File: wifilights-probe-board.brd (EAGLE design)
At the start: 50.8 x 50.8 mm, 48 parts, among them Q1 BUK98180-100A, Q2 BUK98180-100A, Q3 BUK98180-100A, Q4 BUK98180-100A, U2 PCA9685

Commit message: Probe board complete
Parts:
- removed A, B: (no value), adafruit:1X01
- removed B2: DBLS203G, rectifier:DBS
- removed C3: 220pf, resistor:C0805K
- removed C4, C6: 0.1uF, resistor:C0805K
- removed C7: 10uF, resistor:C0805K
- removed D1: MBRS140T3, diode:SMB
- removed L1: 220uf, SparkFun-Passives:SDR0403
- removed LED3: OVSTRGBBCR8, led:OVSTRGBBCR8
- removed MPU: ESP8266_ESP-12, ESP8266-ESP12:ESP8266-ESP12
- removed PWR, THINKING: (no value), led:CHIP-LED0805
- removed Q1, Q2, Q3, Q4: BUK98180-100A, nxp_60:SOT223
- removed R4: 1K, resistor:R0805
- removed R5, R6: 1k, resistor:R0805
- removed R7: ???, resistor:R0805
- removed R8: 10K, resistor:R0805
- removed REG1: MC33063/MC34063D, adafruit:SO08
- removed REG2: MC33269-SO8, linear:SO08
- removed TEMPERATURE: MPL3115A2LGA8, SparkFun-Sensors:LGA8
- removed U$1, U$2, U$3: LUXEON-REBEL, SparkFun-LED:LUXEON-REBEL
- removed U2: PCA9685, adafruit:TSSOP28
- added F1: 500mA, SparkFun:PTC-1206
- added H2, H3, H4, H5: SEW_HOLE, LilyPad-Wearables:SIMPLE_HOLE
- added J1: 22-05-7028-02, con-molex:7395-02
- added JP1: (no value), SparkFun-Connectors:2X5-SHROUDED
- added JP7: USB_MICROB_PLUGCONN-11752, SparkFun-Connectors:USB-B-MICRO-SMD_V03
- added S1: SWITCH-MOMENTARY-2PTH, SparkFun-Electromechanical:TACTILE-PTH
- added TPCHPD, TPGPIO0, TPGPIO2, TPRX, TPTX: (no value), SparkFun-Connectors:1X01_POGOPIN_HOLE_0.58
- added U1: FT232R, SparkFun:SSOP28DB
- C1, C2: device resistor:C0805K -> SparkFun-Capacitors:0603-CAP
- LED1: value OVSTRGBBCR8 -> Red; device led:OVSTRGBBCR8 -> SparkFun-LED:LED-0603
- LED2: value OVSTRGBBCR8 -> Green; device led:OVSTRGBBCR8 -> SparkFun-LED:LED-0603
- P_RED, P_WHITE, RED, SCL, SDA, TP12V, TP3.3V, TP5V, TPGND, WHITE: value TEST-POINT3X5 -> (none); device SparkFun-Passives:PAD.03X.05 -> SparkFun-Connectors:1X01_POGOPIN_HOLE_0.58
- R1: value 220 ??? -> 330; device resistor:R0805 -> SparkFun-Resistors:0603-RES
- R2: value ??? -> 330; device resistor:R0805 -> SparkFun-Resistors:0603-RES
- R3: value 3K -> 1k; device resistor:R0805 -> SparkFun-Passives:AXIAL-0.3
- moved C5 48.8 mm to (49.7, 41.9), flipped to the top, turned to 0 degrees
- moved LED1 39.5 mm to (49.7, 36.8), flipped to the top, turned to 90 degrees
- moved R2 37.2 mm to (49.5, 28.9), flipped to the top, turned to 270 degrees
- moved R1 35.4 mm to (51.8, 28.9), turned to 270 degrees
- moved C2 17.1 mm to (49.7, 44.6), turned to 180 degrees
- moved C1 11.1 mm to (47.5, 28.9), flipped to the top
- moved LED2 9.34 mm to (49.7, 35.6), flipped to the top, turned to 90 degrees
- moved TP3.3V 4.07 mm to (19.7, 24.9)
- moved R3 2.58 mm to (22.5, 20.2), turned to 90 degrees
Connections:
- removed net BLUE: Q2.1, U2.7
- removed net COMP: R3.2, R4.1, REG1.5
- removed net GREEN: Q4.1, U2.9
- removed net N$10: U$1.CATHODE, U$2.ANODE
- removed net N$11: U$2.CATHODE, U$3.ANODE
- removed net N$13: R1.2, REG1.1, REG1.7, REG1.8
- removed net N$14: PWR.A, R2.2
- removed net N$15: R7.2, THINKING.A
- removed net N$16: C3.1, REG1.3
- removed net N$17: C4.1, TEMPERATURE.2
- removed net N$18: A.1, B2.AC1
- removed net N$19: B.1, B2.AC2
- removed net N$20: R8.2, U2.23
- removed net N$25: MPU.13
- removed net N$26: MPU.12
- removed net N$27: MPU.11
- removed net N$28: MPU.10
- removed net N$29: MPU.9
- removed net N$32: MPU.6
- removed net N$33: MPU.4
- removed net N$34: MPU.3
- removed net N$35: MPU.2
- removed net N$36: MPU.5
- removed net N$5: LED2.5, LED2.5@1, LED3.2
- removed net N$6: LED1.5, LED1.5@1, LED2.2
- removed net N$7: LED1.6, LED1.6@1, LED2.3
- removed net N$8: LED2.6, LED2.6@1, LED3.3
- removed net P_BLUE: LED3.6, LED3.6@1, Q2.2, Q2.4
- removed net P_GREEN: LED3.4, LED3.4@1, Q4.2, Q4.4
- removed net RESET: MPU.8
- removed net SWE: D1.C, L1.P$2, REG1.2
- removed net THINKING: MPU.7, R7.1
- new net CTS: U1.11
- new net DCD: U1.10
- new net DSR: U1.9
- new net DTR: U1.2
- new net GPIO0: R3.P$1, S1.3, TPGPIO0.1
- new net N$3: F1.1, JP7.VBUS1
- new net PWREN: U1.14
- new net RI: U1.6
- new net RTS: U1.3
- new net RXD: TPRX.1, U1.5
- new net RXLED: LED2.C, U1.22
- new net SLEEP: U1.12
- new net TXD: TPTX.1, U1.1
- new net TXDEN: U1.13
- new net TXLED: LED1.C, U1.23
- new net USB_D+: JP7.D+1, U1.15
- new net USB_D-: JP7.D-1, U1.16
- new net VCC: C2.1, C5.A, F1.2, U1.20
- net 12V: now also J1.1, TP12V.1; no longer B2.+, LED1.1, LED1.2, LED1.3, R1.1, REG1.6, TP12V.P$1, U$1.ANODE
- net 3.3V: now also JP1.2, R1.2, R2.2, R3.P$2, TP3.3V.1, TPCHPD.1, TPGPIO2.1, U1.17, U1.4; no longer C2.1, C7.1, MPU.16, R2.1, R5.2, R6.2, REG2.2, REG2.3, REG2.6, REG2.7, TEMPERATURE.1, TEMPERATURE.4, TP3.3V.P$1, U2.28
- net 5V: now also JP1.1, TP5V.1; no longer C5.A, C6.1, L1.P$1, R3.1, REG2.4, TP5V.P$1
- net GND: now also H2.P$1, H3.P$1, H4.P$1, H5.P$1, J1.2, JP1.10, JP1.9, JP7.GND1, S1.1, TPGND.1, U1.18, U1.21, U1.25, U1.26, U1.7; no longer B2.-, C3.2, C4.2, C6.2, C7.2, D1.A, MPU.1, PWR.C, Q1.3, Q2.3, Q3.3, Q4.3, R4.2, R8.1, REG1.4, REG2.1, TEMPERATURE.3, THINKING.C, TPGND.P$1, U$1.P$3, U$2.P$3, U$3.P$3, U2.14, U2.25
- net N$1: now also LED1.A, R1.1; no longer LED1.4, LED1.4@1, LED2.1
- net N$2: now also LED2.A, R2.1; no longer LED2.4, LED2.4@1, LED3.1
- net P_RED: now also JP1.8, P_RED.1; no longer LED3.5, LED3.5@1, P_RED.P$1, Q3.2, Q3.4
- net P_WHITE: now also JP1.6, P_WHITE.1; no longer P_WHITE.P$1, Q1.2, Q1.4, U$3.CATHODE
- net RED: now also JP1.7, RED.1; no longer Q3.1, RED.P$1, U2.8
- net SCL: now also JP1.3, SCL.1; no longer MPU.15, R6.1, SCL.P$1, TEMPERATURE.7, U2.26
- net SDA: now also JP1.4, SDA.1; no longer MPU.14, R5.1, SDA.P$1, TEMPERATURE.8, U2.27
- net WHITE: now also JP1.5, WHITE.1; no longer Q1.1, U2.6, WHITE.P$1
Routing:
- net GND: track 128.2 -> 23.8 mm, vias 73 -> 5
- net 12V: track 111.5 -> 27.4 mm, vias 6 -> 0
- net N$11: track 41.7 -> 0.00 mm, vias 2 -> 0
- net N$10: track 41.5 -> 0.00 mm, vias 2 -> 0
- net TXD: track 0.00 -> 38.1 mm
- net N$8: track 37.7 -> 0.00 mm
- net N$7: track 34.9 -> 0.00 mm
- net P_GREEN: track 34.1 -> 0.00 mm, vias 3 -> 0
- net GPIO0: track 0.00 -> 33.0 mm
- net RXD: track 0.00 -> 32.5 mm
- net N$5: track 28.4 -> 0.00 mm
- net N$6: track 27.9 -> 0.00 mm
- net VCC: track 0.00 -> 26.7 mm
- net P_RED: track 24.5 -> 51.1 mm, vias 1 -> 0
- net P_WHITE: track 20.4 -> 45.5 mm, vias 1 -> 0
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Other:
- board size 50.8 x 50.8 mm -> 55.9 x 55.9 mm

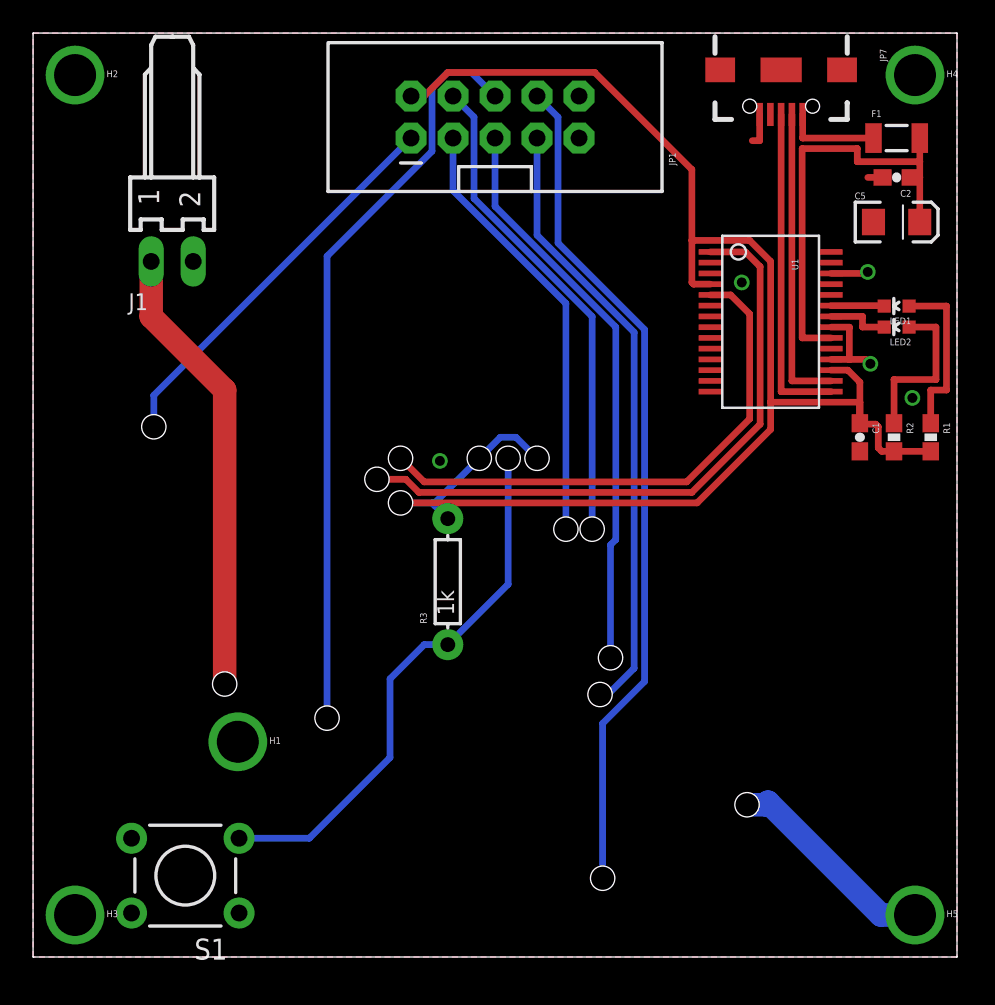
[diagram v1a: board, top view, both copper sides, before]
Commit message: Better probe board
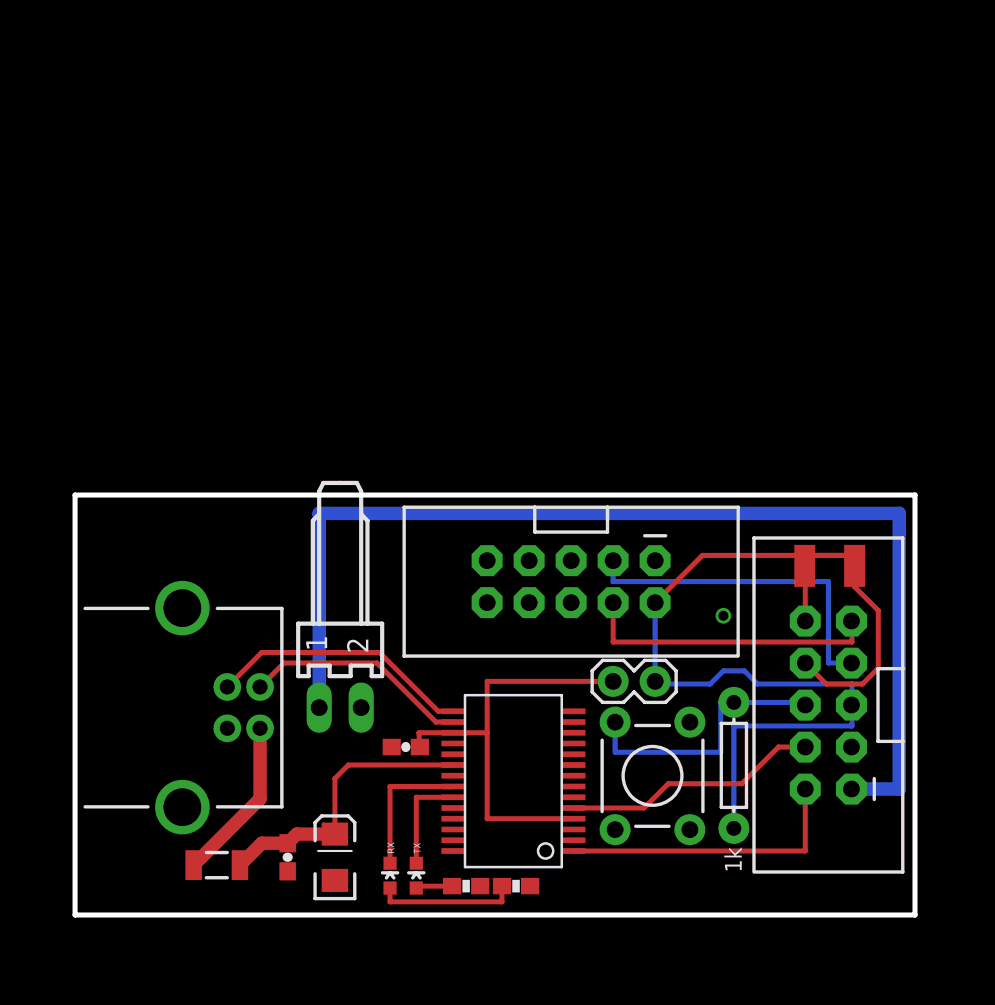
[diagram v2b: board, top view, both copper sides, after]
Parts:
- removed H1, H2, H3, H4, H5: SEW_HOLE, LilyPad-Wearables:SIMPLE_HOLE
- removed JP7: USB_MICROB_PLUGCONN-11752, SparkFun-Connectors:USB-B-MICRO-SMD_V03
- removed LED1: Red, SparkFun-LED:LED-0603
- removed LED2: Green, SparkFun-LED:LED-0603
- removed P_RED, P_WHITE, RED, SCL, SDA, TP12V, TP3.3V, TP5V, TPCHPD, TPGND, TPGPIO0, TPGPIO2, TPRX, TPTX, WHITE: (no value), SparkFun-Connectors:1X01_POGOPIN_HOLE_0.58
- removed R3: 1k, SparkFun-Passives:AXIAL-0.3
- removed S1: SWITCH-MOMENTARY-2PTH, SparkFun-Electromechanical:TACTILE-PTH
- added JP2: (no value), SparkFun-Connectors:2X5-SHROUDED_LOCK
- added JP3: (no value), SparkFun-Retired:1X02
- added JP4: USB-B, SparkFun-Connectors:USB-B-PTH
- added R4: 1k, SparkFun-Passives:AXIAL-0.3
- added RX: Green, SparkFun-LED:LED-0603
- added S2: SWITCH-MOMENTARY-2PTH, SparkFun-Electromechanical:TACTILE-PTH
- added SH1, SH2: SHORT-HT5, shorts-old:SHORT_TOP-50
- added TX: Red, SparkFun-LED:LED-0603
- moved F1 60.2 mm to (8.57, 3.02)
- moved C2 55.2 mm to (12.9, 3.49), turned to 270 degrees
- moved C5 51.3 mm to (15.7, 3.49), turned to 90 degrees
- moved R1 39.1 mm to (23.7, 1.75), turned to 0 degrees
- moved R2 35.5 mm to (26.7, 1.75), turned to 0 degrees
- moved C1 33.2 mm to (20.0, 10.2), turned to 180 degrees
- moved U1 31.8 mm to (26.5, 8.10), turned to 90 degrees
- moved J1 28.8 mm to (16.0, 12.5)
- moved JP1 28.5 mm to (30.0, 20.2), turned to 270 degrees
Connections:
- new net 3.3V-INT: C1.1, JP3.2, U1.17, U1.4
- new net CH_PD: JP2.10, SH2.1
- new net GPIO2: JP2.8, SH1.1
- new net N$4: R1.2
- new net N$5: R2.2
- net 12V: now also JP2.1; no longer TP12V.1
- net 3.3V: now also JP2.5, JP3.1, R4.P$2, SH1.2, SH2.2; no longer C1.1, R1.2, R2.2, R3.P$2, TP3.3V.1, TPCHPD.1, TPGPIO2.1, U1.17, U1.4
- net 5V: no longer TP5V.1
- net GND: now also JP2.3, JP4.GND, S2.1; no longer H1.P$1, H2.P$1, H3.P$1, H4.P$1, H5.P$1, JP7.GND1, S1.1, TPGND.1
- net GPIO0: now also JP2.6, R4.P$1, S2.3; no longer R3.P$1, S1.3, TPGPIO0.1
- net N$1: now also TX.A; no longer LED1.A
- net N$2: now also RX.A; no longer LED2.A
- net N$3: now also JP4.VBUS; no longer JP7.VBUS1
- net P_RED: no longer P_RED.1
- net P_WHITE: no longer P_WHITE.1
- net RED: no longer RED.1
- net RXD: now also JP2.4; no longer TPRX.1
- net RXLED: now also RX.C; no longer LED2.C
- net SCL: now also JP2.7; no longer SCL.1
- net SDA: now also JP2.9; no longer SDA.1
- net TXD: now also JP2.2; no longer TPTX.1
- net TXLED: now also TX.C; no longer LED1.C
- net USB_D+: now also JP4.D+; no longer JP7.D+1
- net USB_D-: now also JP4.D-; no longer JP7.D-1
- net WHITE: no longer WHITE.1
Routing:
- net P_RED: track 51.1 -> 0.00 mm
- net 3.3V: track 96.4 -> 49.7 mm
- net P_WHITE: track 45.5 -> 0.00 mm
- net 12V: track 27.4 -> 66.4 mm
- net RED: track 37.2 -> 0.00 mm
- net WHITE: track 34.6 -> 0.00 mm
- net 3.3V-INT: track 0.00 -> 26.2 mm
- net 5V: track 23.9 -> 0.00 mm
- net GND: track 23.8 -> 0.00 mm, vias 5 -> 1
- net TXD: track 38.1 -> 17.7 mm
- net RXD: track 32.5 -> 15.5 mm
- net GPIO0: track 33.0 -> 16.5 mm
- net SDA: track 29.7 -> 18.1 mm
- net GPIO2: track 0.00 -> 11.5 mm
- net VCC: track 26.7 -> 17.4 mm
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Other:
- board size 55.9 x 55.9 mm -> 50.8 x 25.4 mm

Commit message: Mk6 complete & DRC'd
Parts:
- removed J1: 22-05-7028-02, con-molex:7395-02
- removed JP2: (no value), SparkFun-Connectors:2X5-SHROUDED_LOCK
- removed JP3: (no value), SparkFun-Retired:1X02
- removed JP4: USB-B, SparkFun-Connectors:USB-B-PTH
- removed R4: 1k, SparkFun-Passives:AXIAL-0.3
- removed S2: SWITCH-MOMENTARY-2PTH, SparkFun-Electromechanical:TACTILE-PTH
- removed SH1, SH2: SHORT-HT5, shorts-old:SHORT_TOP-50
- added CN1: (no value), adafruit:USB-MINIB
- added PROGRAM: (no value), SparkFun-Electromechanical:SWITCH-SPST-SMD-A
- added RESET: SWITCH-MOMENTARY-2PTH, SparkFun-Electromechanical:TACTILE-PTH
- added X1: 53261-06, con-molex:53261-06
- C1, C2: device SparkFun-Capacitors:0603-CAP -> SparkFun-Passives:1206
- JP1: value (none) -> 12V DC; device SparkFun-Connectors:2X5-SHROUDED -> SparkFun-Connectors:JST-2-PTH-VERT
- R1, R2: device SparkFun-Resistors:0603-RES -> SparkFun-Passives:1206
- RX: value Green -> GREEN; device SparkFun-LED:LED-0603 -> SparkFun-LED:LED-1206
- TX: value Red -> RED; device SparkFun-LED:LED-0603 -> SparkFun-LED:LED-1206
- moved R1 16.1 mm to (11.9, 12.7), turned to 180 degrees
- moved R2 11.0 mm to (26.8, 12.7)
- moved TX 10.9 mm to (17.0, 12.7)
- moved RX 10.8 mm to (22.1, 12.7), turned to 180 degrees
- moved JP1 8.41 mm to (34.4, 13.0), turned to 0 degrees
- moved F1 6.55 mm to (11.1, 9.05), turned to 90 degrees
- moved C2 5.58 mm to (13.3, 9.05)
- moved C5 5.56 mm to (15.9, 9.05)
- moved U1 2.42 mm to (25.2, 6.03), turned to 0 degrees
- moved C1 1.81 mm to (18.6, 9.05), turned to 270 degrees
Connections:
- removed net 3.3V-INT: C1.1, JP3.2, U1.17, U1.4
- removed net 5V: JP1.1
- removed net CH_PD: JP2.10, SH2.1
- removed net GPIO0: JP2.6, R4.P$1, S2.3
- removed net GPIO2: JP2.8, SH1.1
- removed net N$4: R1.2
- removed net N$5: R2.2
- removed net P_RED: JP1.8
- removed net P_WHITE: JP1.6
- removed net RED: JP1.7
- removed net SCL: JP1.3, JP2.7
- removed net SDA: JP1.4, JP2.9
- removed net WHITE: JP1.5
- net 12V: now also JP1.2, X1.6; no longer J1.1, JP2.1
- net 3.3V: now also C1.1, R1.2, R2.2, U1.17, U1.4; no longer JP1.2, JP2.5, JP3.1, R4.P$2, SH1.2, SH2.2
- net DTR: now also PROGRAM.2, X1.4
- net GND: now also CN1.GND, JP1.1, PROGRAM.3, RESET.3, X1.5; no longer J1.2, JP1.10, JP1.9, JP2.3, JP4.GND, S2.1
- net N$3: now also CN1.VBUS; no longer JP4.VBUS
- net RTS: now also RESET.1, X1.3
- net RXD: now also X1.2; no longer JP2.4
- net TXD: now also X1.1; no longer JP2.2
- net USB_D+: now also CN1.D+; no longer JP4.D+
- net USB_D-: now also CN1.D-; no longer JP4.D-
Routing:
- net 12V: track 66.4 -> 5.13 mm
- net DTR: track 0.00 -> 35.8 mm
- net RTS: track 0.00 -> 35.2 mm
- net TXD: track 17.7 -> 51.2 mm
- net 3.3V-INT: track 26.2 -> 0.00 mm
- net USB_D+: track 16.0 -> 38.5 mm
- net USB_D-: track 13.7 -> 35.4 mm
- net SCL: track 20.6 -> 0.00 mm
- net SDA: track 18.1 -> 0.00 mm
- net GPIO0: track 16.5 -> 0.00 mm
- net GPIO2: track 11.5 -> 0.00 mm
- net N$2: track 8.56 -> 1.86 mm
- net VCC: track 17.4 -> 23.8 mm
- net N$3: track 9.94 -> 5.05 mm
- net RXD: track 15.5 -> 19.2 mm
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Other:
- board size 50.8 x 25.4 mm -> 44.9 x 15.7 mm
